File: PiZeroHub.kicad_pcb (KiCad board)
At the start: 2 copper layers, 65 x 26 mm, 28 parts, among them CON1 BARREL_JACK, P1 USB_OTG, P2 USB_OTG, P3 USB_B, P4 USB_B, P5 USB_B, P6 USB_B, P7 USB_OTG, U1 FE1_1_4PORTUSB, U2 LM7805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

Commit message: Finish first version
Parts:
- added C10: 100uF, Capacitors_SMD:c_elec_5x5.3, F.Cu at (143.3, 81.0)
- added C11: 100uF, Capacitors_SMD:c_elec_5x5.3, F.Cu at (143.3, 89.5)
- added C8: 100uF, Capacitors_SMD:c_elec_5x5.3, F.Cu at (108.8, 81.0)
- added C9: 100uF, Capacitors_SMD:c_elec_5x5.3, F.Cu at (126.0, 81.0)
- added F1: 1A, Fuse_Holders_and_Fuses:Fuse_SMD1206_Wave, F.Cu at (154.9, 80.0)
- added F2: 1.5A, Fuse_Holders_and_Fuses:Fuse_SMD1206_Wave, F.Cu at (132.0, 90.0)
- added REF**: MountingHole_2.4mm, project_footprints:MountingHole_2.4mm, F.Cu at (103.0, 97.0)
- added REF**: MountingHole_2.4mm, project_footprints:MountingHole_2.4mm, F.Cu at (156.0, 76.5)
- U2: footprint project_footprints:sot223 -> project_footprints:sot223_2Output
- moved R2 16.4 mm to (127.0, 84.5), turned to 0 degrees
- moved C5 14.5 mm to (125.5, 87.7), turned to 0 degrees
- moved C4 13.5 mm to (126.7, 86.1), turned to 180 degrees
- moved C1 11.0 mm to (109.7, 87.0), turned to 0 degrees
- moved R1 6.83 mm to (130.3, 98.1), turned to 90 degrees
- moved D5 6.50 mm to (105.5, 87.0), turned to 270 degrees
- moved C3 5.73 mm to (112.0, 92.3)
- moved C2 5.12 mm to (113.8, 92.6)
- moved R5 4.03 mm to (105.5, 90.0), turned to 270 degrees
- moved R4 3.54 mm to (105.5, 92.0)
- moved Y1 3.24 mm to (127.5, 94.2), turned to 0 degrees
- moved D1 2.06 mm to (102.5, 87.0)
- moved D2 2.06 mm to (102.5, 89.0)
- moved D3 2.06 mm to (102.5, 91.0)
- moved D4 2.06 mm to (102.5, 93.0)
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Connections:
- net Net-(U1-Pad2) renamed /X-
- net Net-(U1-Pad3) renamed /X+
- C7 pad 1: +5V -> Net-(C7-Pad1)
- P7 pad 1: +5V -> Net-(F1-Pad1)
- R1 pad 1: Net-(P2-Pad1) -> GND
- U2 pad 2: +5V -> Net-(C7-Pad1)
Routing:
- net +5V: track 0.00 -> 101.4 mm, vias 0 -> 9
- net GND: track 0.00 -> 46.7 mm, vias 0 -> 24
- net Net-(P5-Pad2): track 0.00 -> 29.5 mm
- net +3V3: track 0.00 -> 29.4 mm, vias 0 -> 2
- net Net-(P5-Pad3): track 0.00 -> 25.2 mm
- net Net-(C6-Pad1): track 0.00 -> 24.8 mm
- net Net-(P6-Pad2): track 0.00 -> 24.2 mm
- net Net-(P4-Pad2): track 0.00 -> 23.8 mm
- net Net-(P3-Pad3): track 0.00 -> 22.9 mm
- net Net-(P6-Pad3): track 0.00 -> 22.1 mm
- net Net-(D1-Pad2): track 0.00 -> 22.0 mm
- net Net-(P3-Pad2): track 0.00 -> 20.8 mm
- net Net-(P4-Pad3): track 0.00 -> 20.0 mm
- net Net-(P2-Pad3): track 0.00 -> 19.7 mm
- net Net-(R3-Pad2): track 0.00 -> 19.3 mm, vias 0 -> 3
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- added copper zone on F.Cu, net Net-(C7-Pad1)
- added copper zone on F.Cu, net Net-(F1-Pad1)

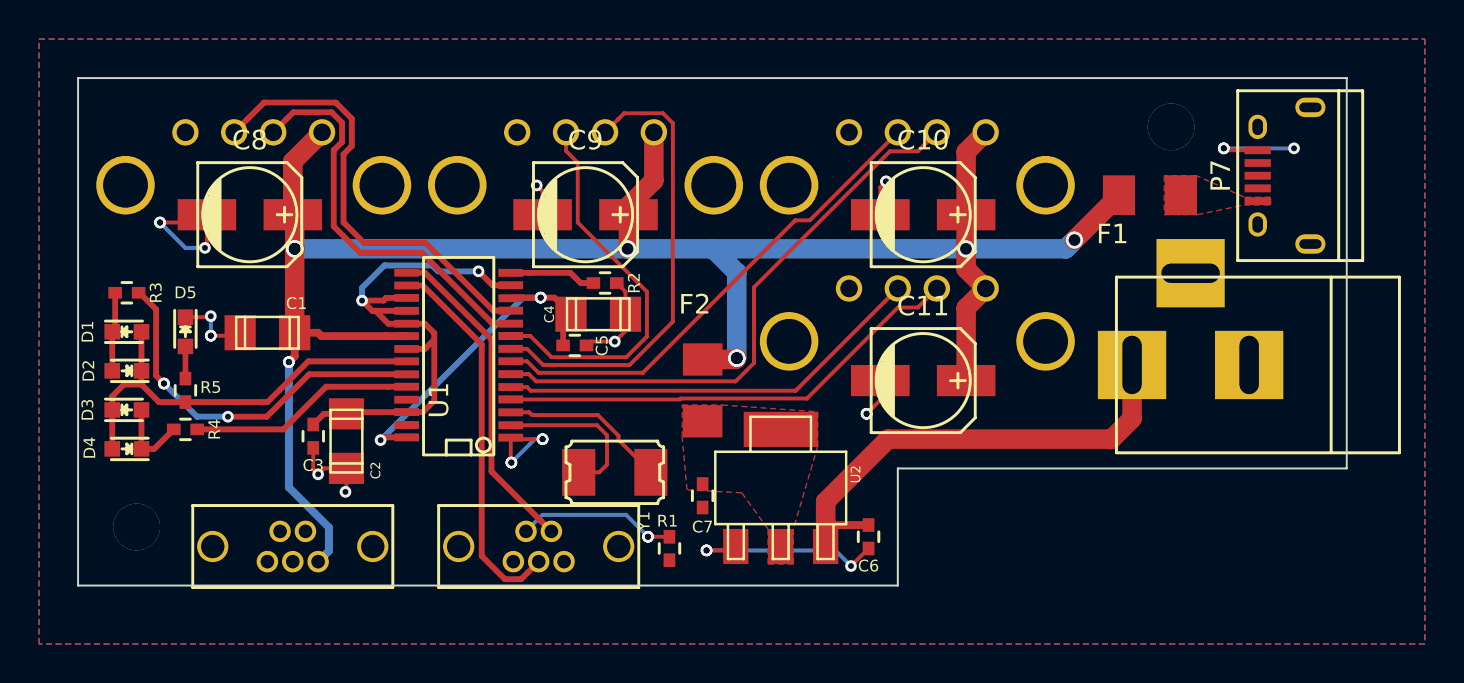
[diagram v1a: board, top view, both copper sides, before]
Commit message: latest version, new USB part and footprint, cleaner design
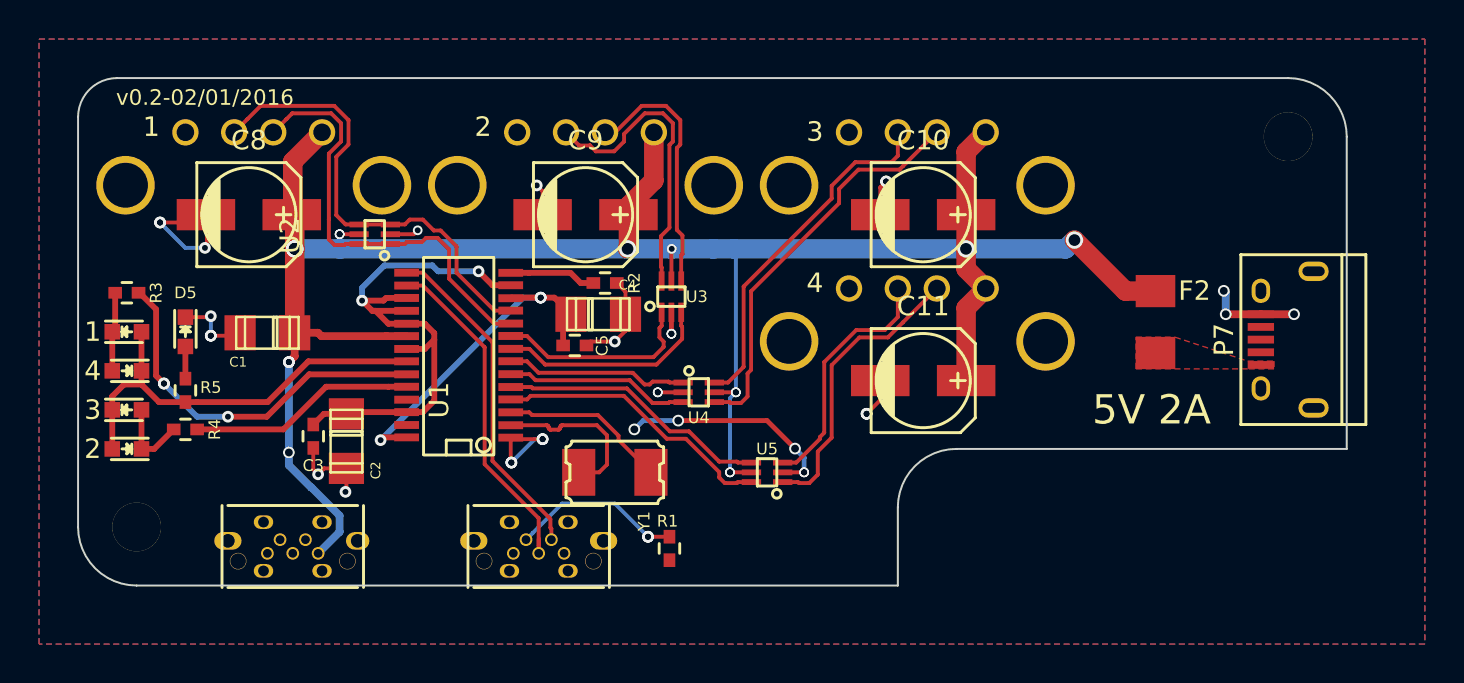
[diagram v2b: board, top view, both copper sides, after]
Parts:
- removed C6: 0.33uF, project_footprint:C_0402_Hand
- removed C7: 0.1uF, project_footprint:C_0402_Hand
- removed CON1: BARREL_JACK, Connect:BARREL_JACK
- removed F1: 1A, Fuse_Holders_and_Fuses:Fuse_SMD1206_Wave
- added G***: LOGO, project_footprints:IdlehandsdevLogo, B.Cu at (137.8, 96.8)
- added G***: LOGO, project_footprints:OSHLogo, B.Cu at (131.4, 97.0)
- added U3: USBLC6-2, project_footprints:SOT-666, F.Cu at (130.4, 85.2)
- added U4: USBLC6-2, project_footprints:SOT-666, F.Cu at (131.8, 90.1)
- added U5: USBLC6-2, project_footprints:SOT-666, F.Cu at (135.3, 94.2)
- C1, C2, C4: footprint project_footprint:c_1206 -> project_footprints:c_1206_pol
- F2: value 1.5A -> 2A
- P1, P2: footprint project_footprints:USB_Micro-B_Vert_OTG -> project_footprints:USBOTG_BoardMount
- P7: value USB_OTG -> USB_POWER
- REF** (x2): footprint project_footprints:MountingHole_2.4mm -> project_footprints:MountingHole_2.5mm
- U2: value LM7805 -> USBLC6-2; footprint project_footprints:sot223_2Output -> project_footprints:SOT-666
- moved U2 24.5 mm to (115.2, 82.0), turned to 90 degrees
- moved F2 23.5 mm to (155.2, 86.5)
- moved P7 8.40 mm to (162.2, 87.4)
- moved REF** 6.02 mm to (162.0, 77.0)
- moved C8 0.05 mm to (108.8, 81.0)
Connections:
- net Net-(P4-Pad2) renamed /D2-
- net Net-(P4-Pad3) renamed /D2+
- net Net-(P5-Pad2) renamed /D3-
- net Net-(P5-Pad3) renamed /D3+
- net Net-(P6-Pad2) renamed /D4-
- net Net-(P6-Pad3) renamed /D4+
- F2 pad 1: Net-(C7-Pad1) -> Net-(F2-Pad1)
- P3 pad 2: Net-(P3-Pad2) -> /D1-
- P3 pad 3: Net-(P3-Pad3) -> /D1+
- P7 pad 1: Net-(F1-Pad1) -> Net-(F2-Pad1)
- U1 pad 10: Net-(P3-Pad2) -> /D1-
- U1 pad 11: Net-(P3-Pad3) -> /D1+
- U2 pad 1: GND -> /D1-
- U2 pad 2: Net-(C7-Pad1) -> GND
- U2 pad 3: Net-(C6-Pad1) -> /D1+
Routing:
- net Net-(C6-Pad1): track 24.8 -> 0.00 mm
- net /D1+: track 0.00 -> 23.8 mm
- net Net-(P3-Pad3): track 22.9 -> 0.00 mm
- net /D1-: track 0.00 -> 22.6 mm
- net Net-(P3-Pad2): track 20.8 -> 0.00 mm
- net +5V: track 101.4 -> 112.8 mm, vias 9 -> 15
- net /D2+: track 20.0 -> 25.9 mm
- net /D4-: track 24.2 -> 29.4 mm
- net /D4+: track 22.1 -> 26.6 mm
- net GND: track 46.7 -> 50.9 mm, vias 24 -> 31
- net /D3+: track 25.2 -> 27.6 mm
- net Net-(P2-Pad3): track 19.7 -> 17.4 mm
- net /D2-: track 23.8 -> 25.1 mm
- net Net-(P2-Pad4): track 8.17 -> 8.82 mm
- net /D3-: track 29.5 -> 30.1 mm
- added copper zone on F.Cu, net Net-(F2-Pad1)
- removed copper zone on F.Cu, net Net-(C7-Pad1)
- removed copper zone on F.Cu, net Net-(F1-Pad1)
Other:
- outline, holes or cut-outs redrawn
- net class Default: clearance 0.2 -> 0.15
- rule trace_clearance: 0.2 -> 0.15
- board text added: "1"
- board text added: "2"
- board text added: "3"
- board text added: "4"
- board text added: "5V 2A"
- board text added: "PWR"
- board text added: "Pi Powered Hub Zero Idle Hands Dev."
- board text added: "USB"
- board text added: "v0.2-02/01/2016"
